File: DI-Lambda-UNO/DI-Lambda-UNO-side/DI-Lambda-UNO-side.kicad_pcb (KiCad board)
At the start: 2 copper layers, 125 x 28.2 mm, 0 parts

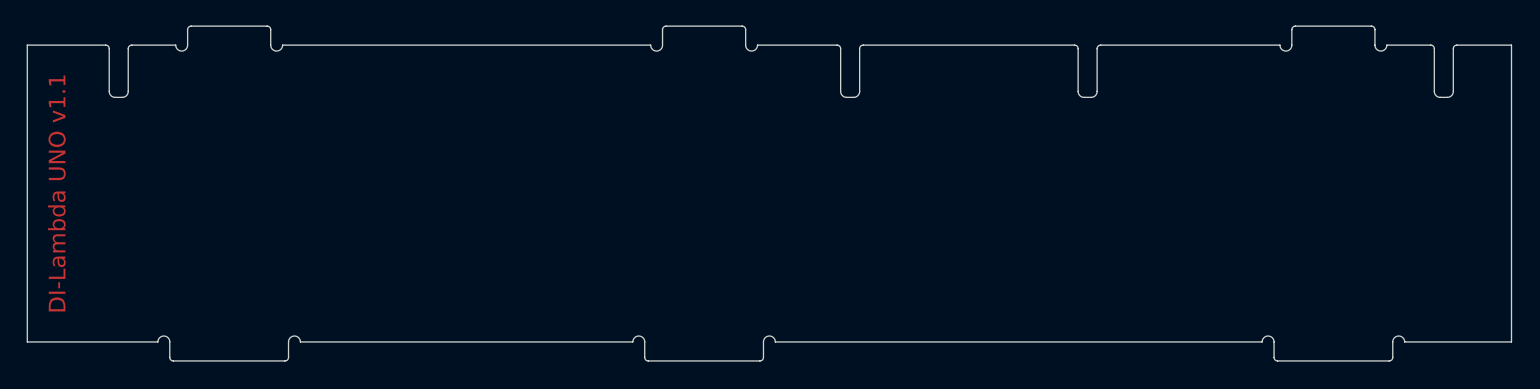
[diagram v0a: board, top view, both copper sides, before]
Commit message: Copper pour on the side boards
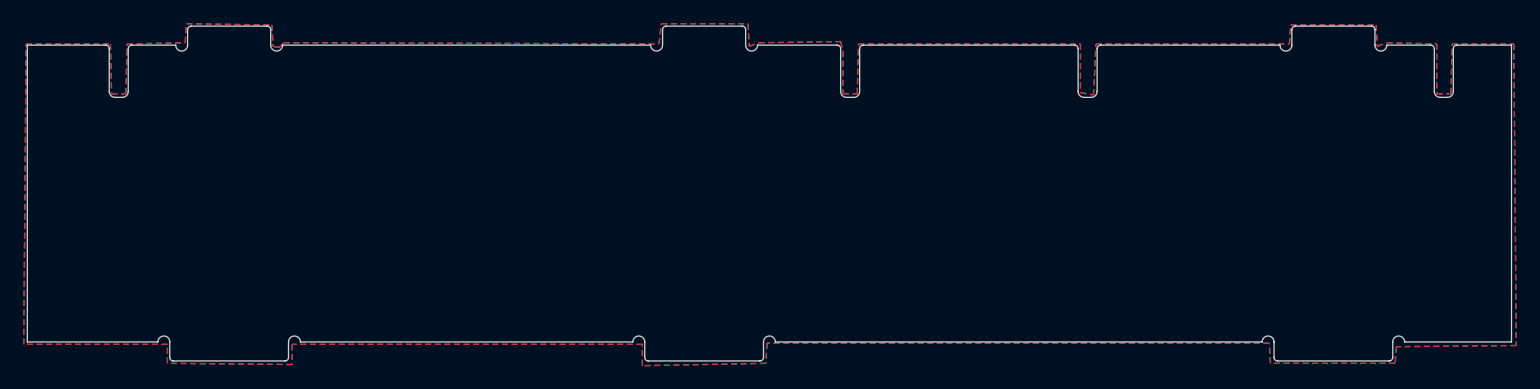
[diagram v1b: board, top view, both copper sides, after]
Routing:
- added copper zone on B.Cu, net (none)
- added copper zone on F.Cu, net (none)
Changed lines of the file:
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@@
     (0 F.Cu signal)
     (31 B.Cu signal)
-    (32 B.Adhes user hide)
-    (33 F.Adhes user hide)
-    (34 B.Paste user hide)
-    (35 F.Paste user hide)
-    (36 B.SilkS user hide)
+    (32 B.Adhes user)
+    (33 F.Adhes user)
+    (34 B.Paste user)
+    (35 F.Paste user)
+    (36 B.SilkS user)
     (37 F.SilkS user)
-    (38 B.Mask user hide)
-    (39 F.Mask user hide)
+    (38 B.Mask user)
+    (39 F.Mask user)
     (40 Dwgs.User user)
     (41 Cmts.User user)
@@
     (47 F.CrtYd user)
     (48 B.Fab user)
-    (49 F.Fab user hide)
+    (49 F.Fab user)
   )
   (setup
@@
     (visible_elements FFFDFF7F)
     (pcbplotparams
-      (layerselection 0x000c0_ffffffff)
+      (layerselection 0x010c0_ffffffff)
       (usegerberextensions true)
       (usegerberattributes true)
@@
       (drillshape 0)
       (scaleselection 1)
-      (outputdirectory DI-Lambda-UNO-side-v1.0-gerbers-20170824/))
+      (outputdirectory DI-Lambda-UNO-side-v1.0-gerbers-2017oct25/))
   )
   (net 0 "")
@@
     (arrow2b (pts (xy 95.08 81.51) (xy 96.206504 80.923579)))
   )
-  (gr_text "DI-Lambda UNO v1.1" (at 97.64 64.01 90) (layer F.Cu)
+  (gr_text "DI-Lambda UNO v1.1" (at 97.64 64.01 90) (layer F.Mask)
     (effects (font (size 1.4 1.4) (thickness 0.28)))
   )
@@
   (gr_line (start 103.08 55.91) (end 102.48 55.91) (layer Edge.Cuts) (width 0.1))
   (gr_line (start 103.58 51.81) (end 103.58 55.41) (layer Edge.Cuts) (width 0.1))
+  (zone (net 0) (net_name "") (layer F.Cu) (hatch edge 0.508)
+    (connect_pads (clearance 0.508))
+    (min_thickness 0.254)
+    (fill yes (arc_segments 16) (thermal_gap 0.508) (thermal_bridge_width 0.508))
+    (polygon
+      (pts
+        (xy 94.98 51.41) (xy 102.08 51.41) (xy 102.18 55.61) (xy 103.38 55.61) (xy 103.48 51.41)
+        (xy 108.38 51.31) (xy 108.48 49.71) (xy 115.68 49.81) (xy 115.78 51.61) (xy 116.28 51.71)
+        (xy 116.68 51.31) (xy 148.28 51.41) (xy 148.48 49.71) (xy 155.78 49.71) (xy 155.88 51.61)
+        (xy 156.68 51.31) (xy 163.58 51.21) (xy 163.78 52.01) (xy 163.78 55.61) (xy 164.98 55.61)
+        (xy 165.08 51.41) (xy 183.78 51.41) (xy 183.78 55.51) (xy 184.88 55.71) (xy 185.08 51.41)
+        (xy 201.38 51.41) (xy 201.48 49.81) (xy 208.68 49.81) (xy 208.78 51.61) (xy 209.58 51.31)
+        (xy 213.78 51.41) (xy 213.78 55.61) (xy 214.98 55.61) (xy 215.08 51.41) (xy 220.28 51.41)
+        (xy 220.48 76.81) (xy 210.38 76.91) (xy 210.28 78.31) (xy 199.78 78.31) (xy 199.68 76.61)
+        (xy 157.38 76.61) (xy 157.28 78.31) (xy 146.88 78.51) (xy 146.88 76.71) (xy 117.38 76.71)
+        (xy 117.38 78.41) (xy 106.88 78.31) (xy 106.88 76.71) (xy 94.78 76.71)
+      )
+    )
+  )
+  (zone (net 0) (net_name "") (layer B.Cu) (hatch edge 0.508)
+    (connect_pads (clearance 0.508))
+    (min_thickness 0.254)
+    (fill yes (arc_segments 16) (thermal_gap 0.508) (thermal_bridge_width 0.508))
+    (polygon
+      (pts
+        (xy 94.98 51.41) (xy 102.08 51.41) (xy 102.18 55.61) (xy 103.38 55.61) (xy 103.48 51.41)
+        (xy 108.38 51.31) (xy 108.48 49.71) (xy 115.68 49.81) (xy 115.78 51.61) (xy 116.28 51.71)
+        (xy 116.68 51.31) (xy 148.28 51.41) (xy 148.48 49.71) (xy 155.78 49.71) (xy 155.88 51.61)
+        (xy 156.68 51.31) (xy 163.58 51.21) (xy 163.78 52.01) (xy 163.78 55.61) (xy 164.98 55.61)
+        (xy 165.08 51.41) (xy 183.78 51.41) (xy 183.78 55.51) (xy 184.88 55.71) (xy 185.08 51.41)
+        (xy 201.38 51.41) (xy 201.48 49.81) (xy 208.68 49.81) (xy 208.78 51.61) (xy 209.58 51.31)
+        (xy 213.78 51.41) (xy 213.78 55.61) (xy 214.98 55.61) (xy 215.08 51.41) (xy 220.28 51.41)
+        (xy 220.48 76.81) (xy 210.38 76.91) (xy 210.28 78.31) (xy 199.78 78.31) (xy 199.68 76.61)
+        (xy 157.38 76.61) (xy 157.28 78.31) (xy 146.88 78.51) (xy 146.88 76.71) (xy 117.38 76.71)
+        (xy 117.38 78.41) (xy 106.88 78.31) (xy 106.88 76.71) (xy 94.78 76.71)
+      )
+    )
+  )
 )
